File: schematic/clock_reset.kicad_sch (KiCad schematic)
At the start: 38 parts, among them Q2 2N3906, U22 74LS04, U7 74LS05, U8 74LS74, Y1 7.159090Mhz

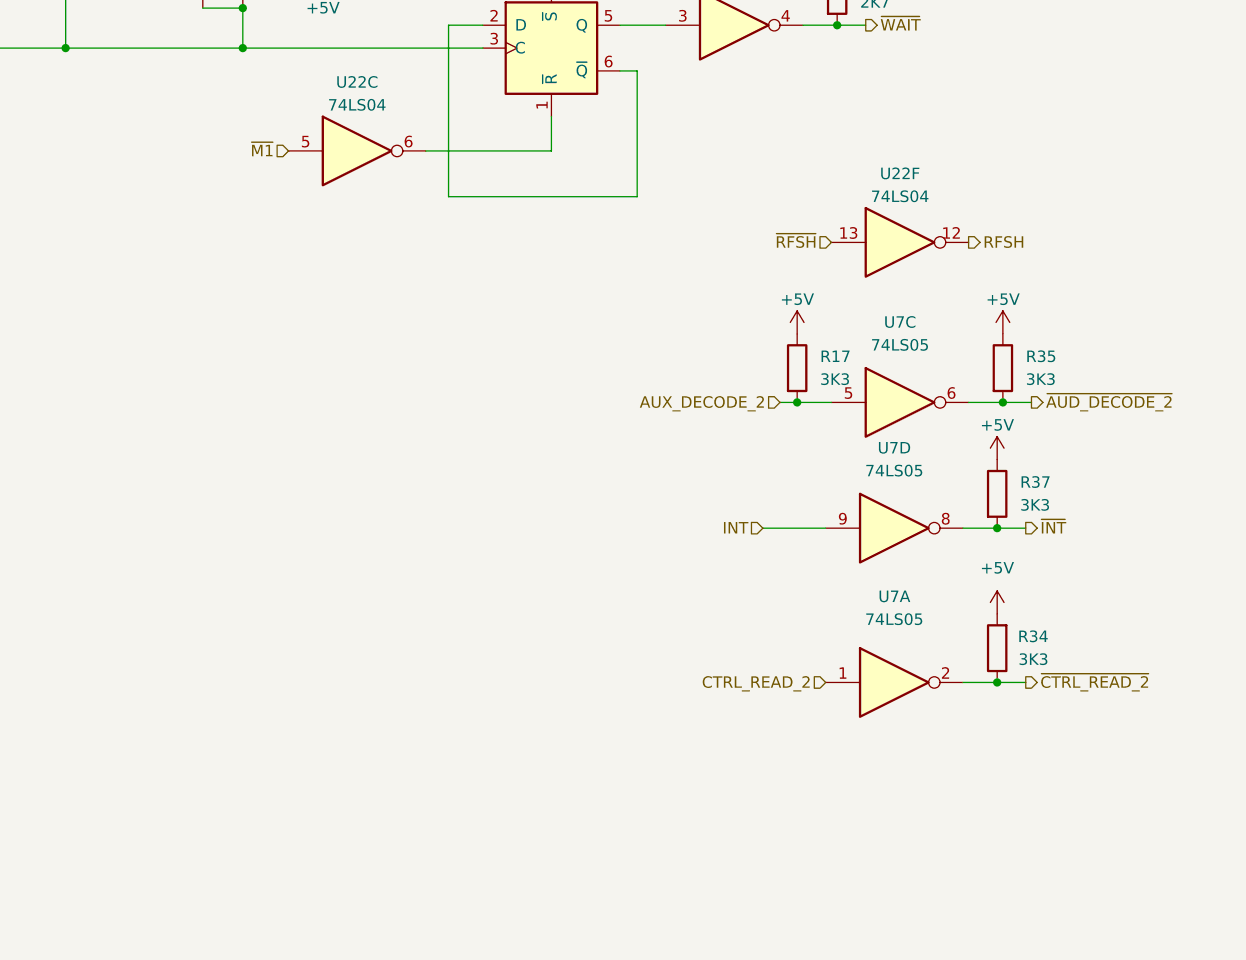
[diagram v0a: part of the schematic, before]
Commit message: adjusted size of the sheets. added pcb version to the rev field. F.0... the 0 is for future fixes on my end. RF PCB is E.0.
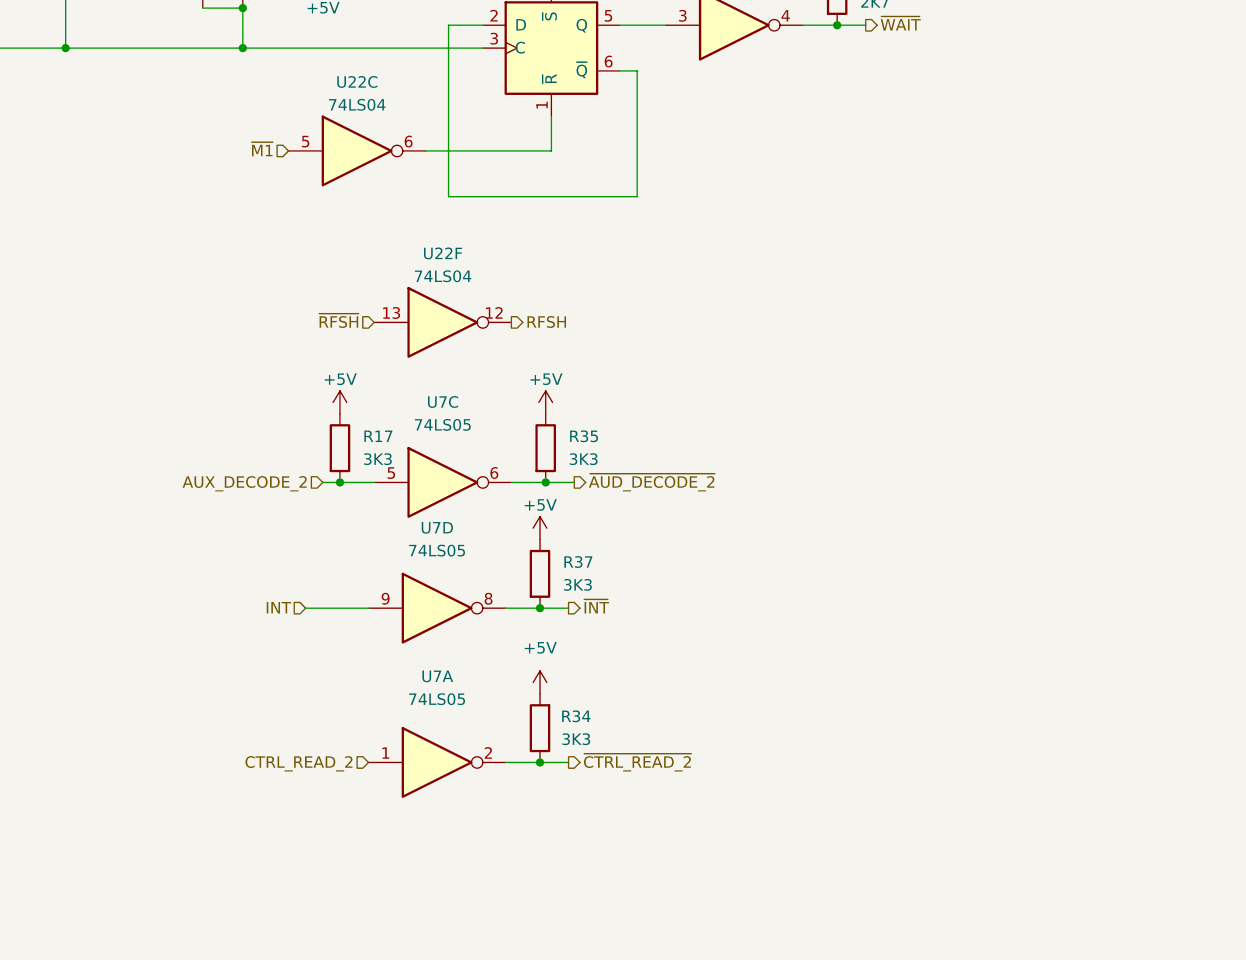
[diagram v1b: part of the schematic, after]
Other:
- title: (none) -> Colecovision Schematic
- moved on the sheet: R17, R34, R35, R37, U22F, U7A, U7C, U7D

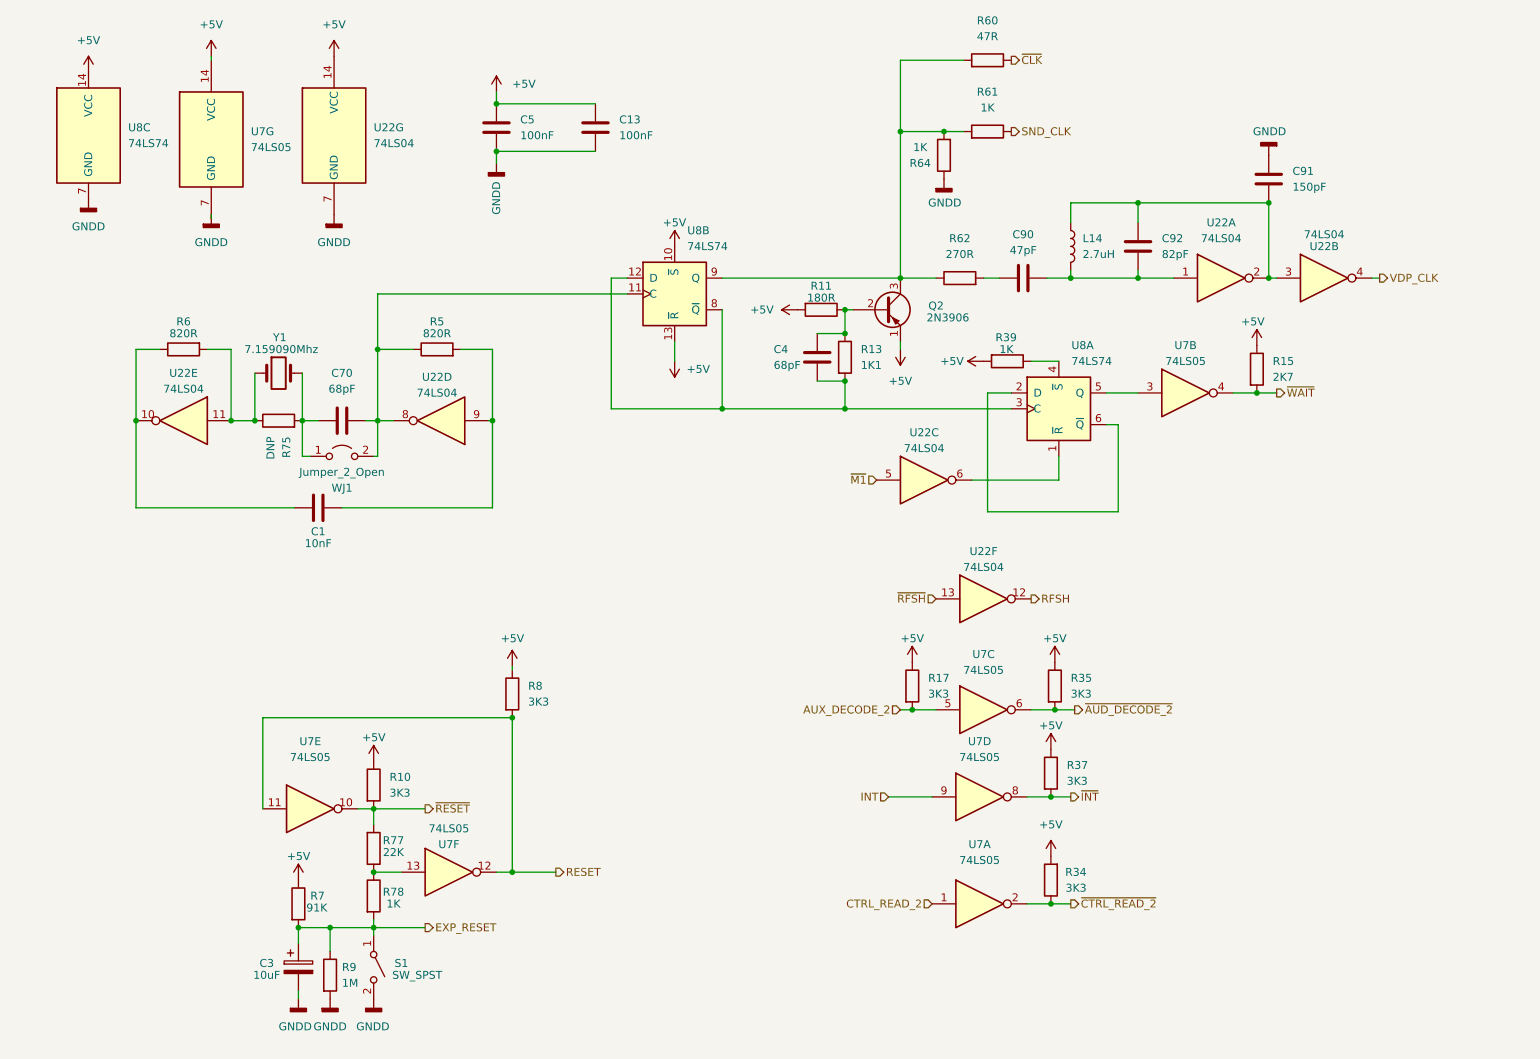
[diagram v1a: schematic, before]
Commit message: cleanup, and started associating components
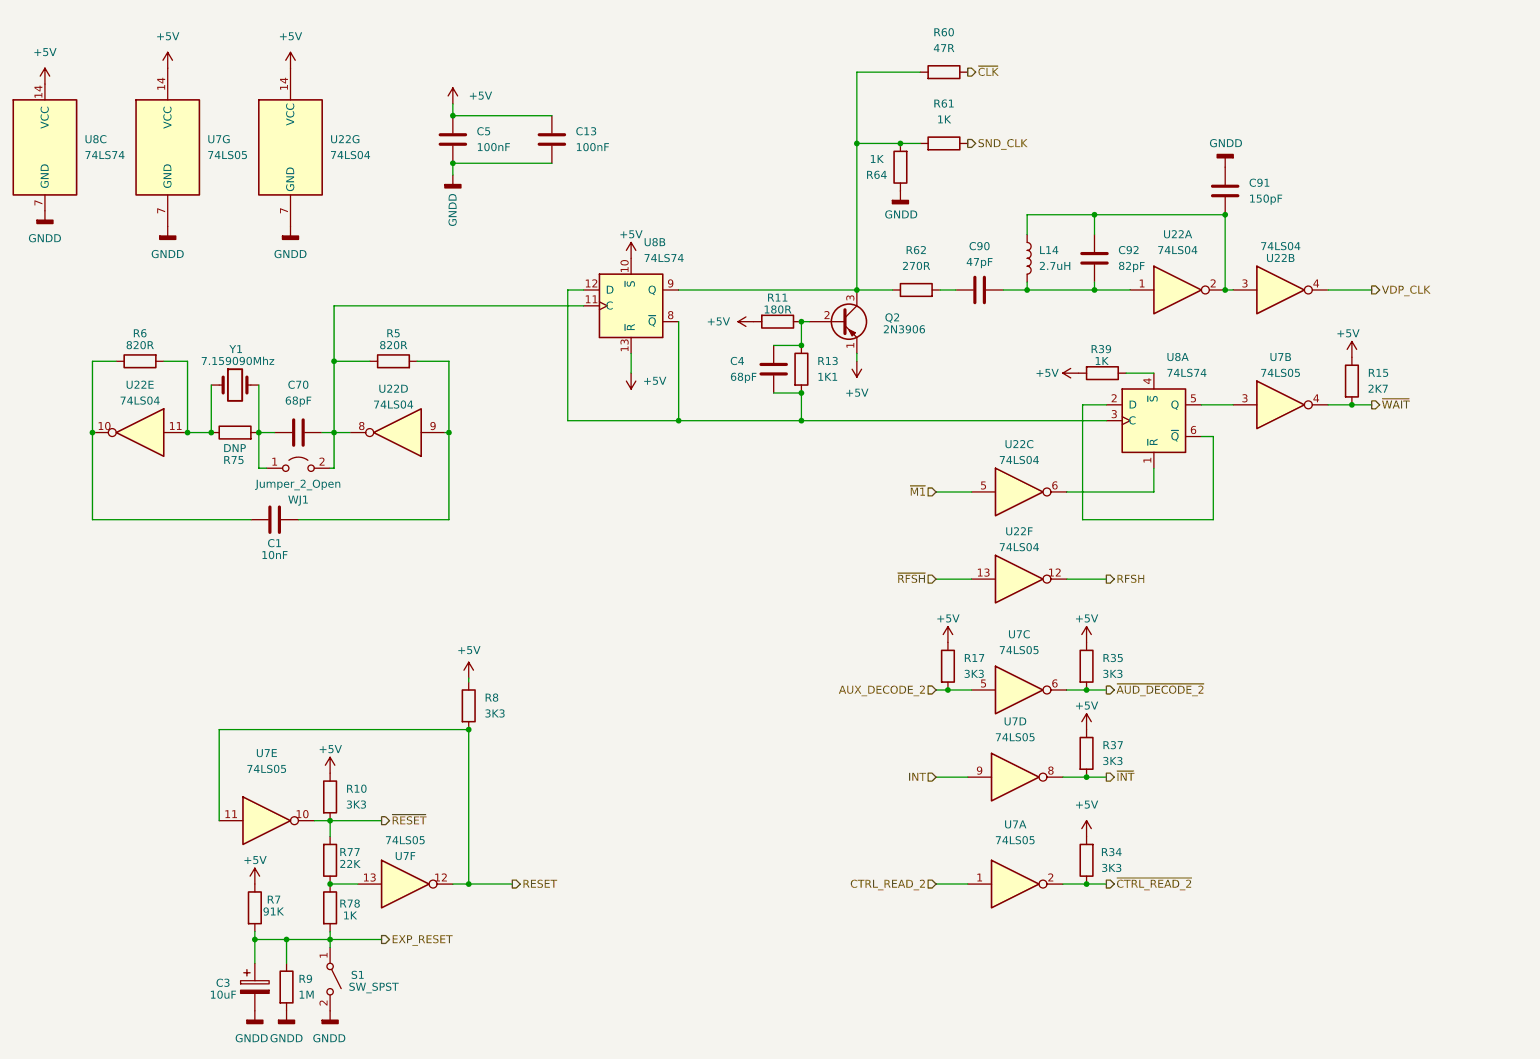
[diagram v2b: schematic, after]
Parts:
- C1, C13, C5: footprint (none) -> Capacitor_THT:C_Disc_D10.0mm_W2.5mm_P5.00mm
- C3: footprint (none) -> Capacitor_THT:CP_Radial_D5.0mm_P2.00mm
- C4, C70, C90, C91, C92: footprint (none) -> Capacitor_THT:C_Disc_D7.0mm_W2.5mm_P5.00mm
- L14: footprint (none) -> Inductor_THT:L_Axial_L12.8mm_D5.8mm_P7.62mm_Vertical_Fastron_HBCC
- Q2: footprint Package_TO_SOT_THT:TO-92_Inline -> Package_TO_SOT_THT:TO-92_Wide
- R10, R11, R13, R15, R17, R34, R35, R37, R39, R5, R6, R60, R61, R62, R64, R7, R75, R77, R78, R8, R9: footprint (none) -> Resistor_THT:R_Axial_DIN0207_L6.3mm_D2.5mm_P7.62mm_Horizontal
- S1: footprint (none) -> Button_Switch_THT:SW_TH_Tactile_Omron_B3F-10xx
- U22, U7, U8: footprint (none) -> Package_DIP:DIP-14_W7.62mm_LongPads
- WJ1: footprint (none) -> Resistor_THT:R_Bare_Metal_Element_L16.3mm_W4.8mm_P15.30mm
- Y1: footprint (none) -> Crystal:Crystal_HC49-U_Vertical
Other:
- moved on the sheet: C1, C13, C3, C4, C5, C70, C90, C91, C92, L14, Q2, R10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

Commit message: added new libs for rest of the parts. some still need updating for correct parts, but for now they work. PCB import complete.
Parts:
- WJ1: footprint Resistor_THT:R_Bare_Metal_Element_L16.3mm_W4.8mm_P15.30mm -> Resistor_THT:R_Axial_DIN0204_L3.6mm_D1.6mm_P7.62mm_Horizontal
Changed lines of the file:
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@@
     (property "Reference" "WJ1" (id 0) (at 74.93 97.155 0))
     (property "Value" "Jumper_2_Open" (id 1) (at 74.93 94.615 0))
-    (property "Footprint" "Resistor_THT:R_Bare_Metal_Element_L16.3mm_W4.8mm_P15.30mm" (id 2) (at 74.93 92.075 0)
+    (property "Footprint" "Resistor_THT:R_Axial_DIN0204_L3.6mm_D1.6mm_P7.62mm_Horizontal" (id 2) (at 74.93 92.075 0)
       (effects (font (size 1.27 1.27)) hide)
     )

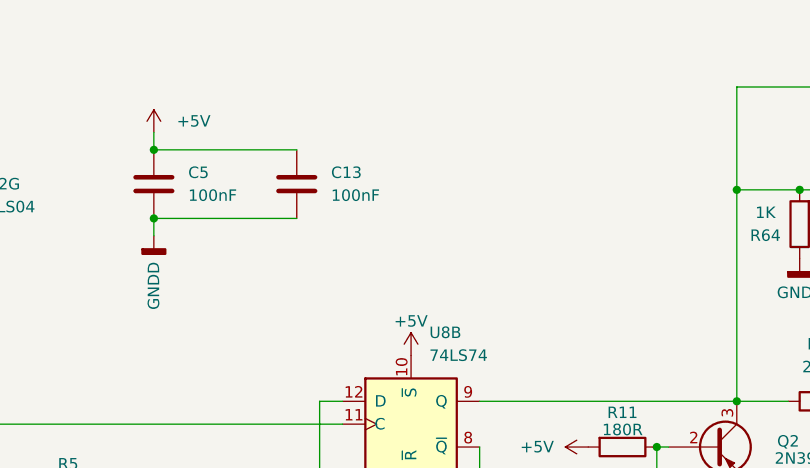
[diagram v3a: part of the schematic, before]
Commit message: first draft of board with components added, no traces
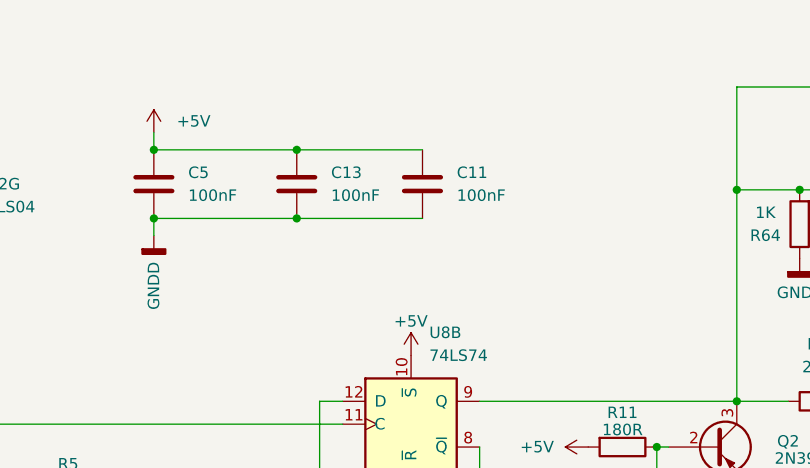
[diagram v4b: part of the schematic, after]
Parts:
- added C11: 100nF, Capacitor_THT:C_Disc_D7.0mm_W2.5mm_P5.00mm, symbol Device:C
- C1, C13, C5: footprint Capacitor_THT:C_Disc_D10.0mm_W2.5mm_P5.00mm -> Capacitor_THT:C_Disc_D7.0mm_W2.5mm_P5.00mm
- C3: footprint Capacitor_THT:CP_Radial_D5.0mm_P2.00mm -> Capacitor_THT:CP_Radial_D5.0mm_P2.50mm
- L14: footprint Inductor_THT:L_Axial_L12.8mm_D5.8mm_P7.62mm_Vertical_Fastron_HBCC -> Inductor_THT:L_Axial_L11.0mm_D4.5mm_P7.62mm_Vertical_Fastron_MECC
- R10, R11, R13, R15, R17, R34, R35, R37, R39, R5, R6, R60, R61, R62, R64, R7, R75, R77, R78, R8, R9: footprint Resistor_THT:R_Axial_DIN0207_L6.3mm_D2.5mm_P7.62mm_Horizontal -> Resistor_THT:R_Axial_DIN0207_L6.3mm_D2.5mm_P10.16mm_Horizontal
- S1: footprint Button_Switch_THT:SW_TH_Tactile_Omron_B3F-10xx -> Switches_THT:Coleco_RST
- WJ1: footprint Resistor_THT:R_Axial_DIN0204_L3.6mm_D1.6mm_P7.62mm_Horizontal -> Resistor_THT:R_Axial_DIN0207_L6.3mm_D2.5mm_P15.24mm_Horizontal
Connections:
- net +5V: now also C11.2
- net GNDD: now also C11.1
